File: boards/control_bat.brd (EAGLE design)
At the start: 102.6 x 30.5 mm, 13 parts, among them U1 MCP1703T-3002E/CB, U3 LPC824M201JDH20J, X2 53398-04

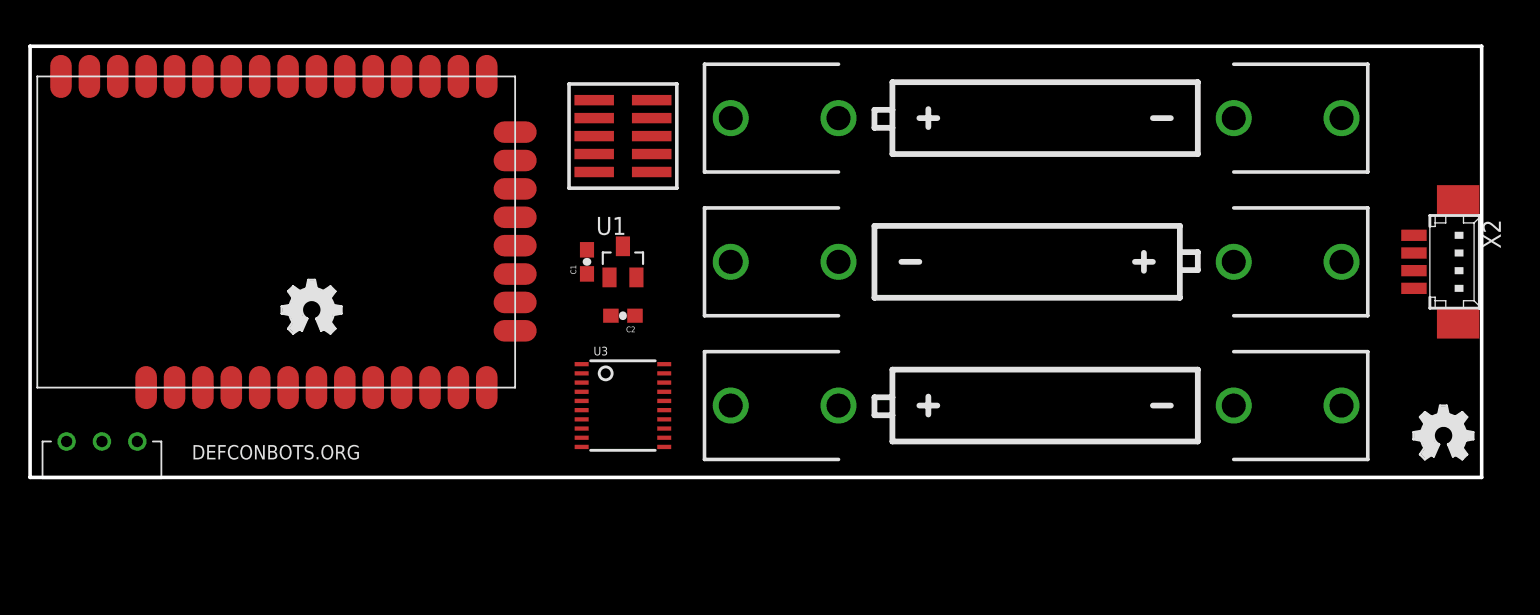
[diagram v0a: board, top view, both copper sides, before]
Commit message: First pass layout of control/battery board
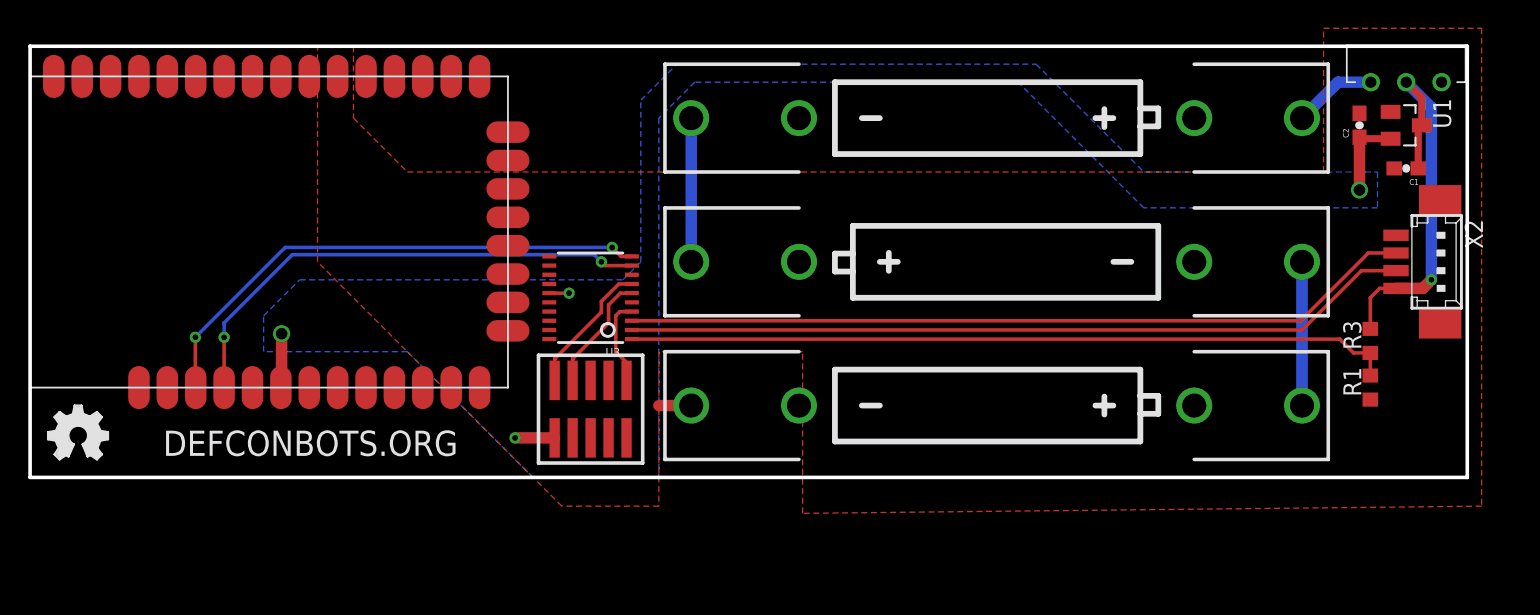
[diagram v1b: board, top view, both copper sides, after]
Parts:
- removed LOGO2: OSHW_LOGO_FILLX0150-NT, ohw-logo:OSHW_FILLX150_NOTEXT
- added R1, R3: 10k, rcl:R0603
- moved LOGO1 96.5 mm to (1.27, 1.27)
- moved S3 95.6 mm to (97.3, 27.9), turned to 90 degrees
- moved C1 58.3 mm to (97.3, 21.8), turned to 180 degrees
- moved U1 56.2 mm to (97.3, 24.9), turned to 270 degrees
- moved C2 53.8 mm to (94.0, 24.9), turned to 90 degrees
- moved BAT1 20.5 mm to (68.3, 5.08), turned to 180 degrees
- moved BAT3 20.5 mm to (68.3, 25.4), turned to 180 degrees
- moved U$3 19.4 mm to (39.6, 4.83), turned to 0 degrees
- moved U3 7.96 mm to (39.6, 12.7), turned to 90 degrees
- moved BAT2 2.79 mm to (68.3, 15.2), turned to 0 degrees
- moved X2 1.27 mm to (99.1, 15.2)
- moved XB1 0.51 mm to (33.8, 6.35)
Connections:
- removed net BLUE_LED: U3.1
- removed net LASER_RX: U3.3
- removed net RED_LED: U3.10
- new net N$3: BAT3.PWR@1, S3.P$1
- new net RF_RX: U3.10, XB1.3
- new net RF_TX: U3.9, XB1.4
- net +3V3: now also XB1.6
- net GND: now also R1.1, XB1.27
- net RX: now also U3.3; no longer U3.8
- net TX: now also U3.2; no longer U3.9
- net VBAT: now also R1.2, R3.1, U3.1; no longer BAT3.PWR@1, S3.P$2
- net VIN: now also R3.2, S3.P$2; no longer S3.P$1
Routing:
- net RX: track 0.00 -> 56.0 mm
- net TX: track 0.00 -> 55.8 mm
- net VBAT: track 0.00 -> 54.2 mm
- net RF_RX: track 0.00 -> 37.3 mm, vias 0 -> 2
- net RF_TX: track 0.00 -> 35.7 mm, vias 0 -> 2
- net VIN: track 0.00 -> 28.4 mm, vias 0 -> 1
- net +3V3: track 0.00 -> 14.0 mm, vias 0 -> 4
- net N$1: track 0.00 -> 10.2 mm
- net N$2: track 0.00 -> 10.2 mm
- net SWDIO: track 0.00 -> 9.62 mm
- net SWCLK: track 0.00 -> 8.38 mm
- net RST: track 0.00 -> 6.15 mm
- net N$3: track 0.00 -> 5.92 mm
- net GND: track 0.00 -> 2.29 mm
- added copper zone on layer 16, net +3V3
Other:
- board size 102.6 x 30.5 mm -> 101.6 x 30.5 mm

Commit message: Add serial debug port on xbee in case I need to configure it manually
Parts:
- added JP1: (no value), SparkFun-Connectors:1X03
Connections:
- net RF_RX: now also JP1.1
- net RF_TX: now also JP1.2
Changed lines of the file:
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@@
 <layer number="98" name="Guide" color="6" fill="1" visible="no" active="no"/>
 <layer number="99" name="SpiceOrder" color="7" fill="1" visible="no" active="no"/>
+<layer number="100" name="Muster" color="7" fill="1" visible="no" active="no"/>
+<layer number="101" name="Patch_Top" color="12" fill="4" visible="no" active="yes"/>
+<layer number="102" name="Vscore" color="7" fill="1" visible="no" active="yes"/>
+<layer number="103" name="tMap" color="7" fill="1" visible="no" active="yes"/>
+<layer number="104" name="Name" color="16" fill="1" visible="no" active="yes"/>
+<layer number="105" name="tPlate" color="7" fill="1" visible="no" active="yes"/>
+<layer number="106" name="bPlate" color="7" fill="1" visible="no" active="yes"/>
+<layer number="107" name="Crop" color="7" fill="1" visible="no" active="yes"/>
+<layer number="108" name="tplace-old" color="10" fill="1" visible="no" active="yes"/>
+<layer number="109" name="ref-old" color="11" fill="1" visible="no" active="yes"/>
+<layer number="110" name="fp0" color="7" fill="1" visible="no" active="yes"/>
 <layer number="111" name="Route11" color="7" fill="1" visible="no" active="no"/>
 <layer number="112" name="Route12" color="7" fill="1" visible="no" active="no"/>
@@
 <layer number="114" name="Route14" color="7" fill="1" visible="no" active="no"/>
 <layer number="115" name="Route15" color="7" fill="1" visible="no" active="no"/>
+<layer number="116" name="Patch_BOT" color="9" fill="4" visible="no" active="yes"/>
+<layer number="121" name="_tsilk" color="7" fill="1" visible="no" active="yes"/>
+<layer number="122" name="_bsilk" color="7" fill="1" visible="no" active="yes"/>
+<layer number="123" name="tTestmark" color="7" fill="1" visible="no" active="yes"/>
+<layer number="124" name="bTestmark" color="7" fill="1" visible="no" active="yes"/>
+<layer number="125" name="_tNames" color="7" fill="1" visible="no" active="yes"/>
+<layer number="126" name="_bNames" color="7" fill="1" visible="no" active="yes"/>
+<layer number="127" name="_tValues" color="7" fill="1" visible="no" active="yes"/>
+<layer number="128" name="_bValues" color="7" fill="1" visible="no" active="yes"/>
+<layer number="131" name="tAdjust" color="7" fill="1" visible="no" active="yes"/>
+<layer number="132" name="bAdjust" color="7" fill="1" visible="no" active="yes"/>
+<layer number="144" name="Drill_legend" color="7" fill="1" visible="no" active="yes"/>
+<layer number="150" name="Notes" color="7" fill="1" visible="no" active="yes"/>
+<layer number="151" name="HeatSink" color="7" fill="1" visible="no" active="yes"/>
+<layer number="152" name="_bDocu" color="7" fill="1" visible="no" active="yes"/>
+<layer number="153" name="FabDoc1" color="7" fill="1" visible="no" active="yes"/>
+<layer number="154" name="FabDoc2" color="7" fill="1" visible="no" active="yes"/>
+<layer number="155" name="FabDoc3" color="7" fill="1" visible="no" active="yes"/>
+<layer number="199" name="Contour" color="7" fill="1" visible="no" active="yes"/>
 <layer number="200" name="200bmp" color="1" fill="10" visible="no" active="no"/>
+<layer number="201" name="201bmp" color="2" fill="10" visible="no" active="yes"/>
+<layer number="202" name="202bmp" color="3" fill="10" visible="no" active="yes"/>
+<layer number="203" name="203bmp" color="4" fill="10" visible="no" active="yes"/>
+<layer number="204" name="204bmp" color="5" fill="10" visible="no" active="yes"/>
+<layer number="205" name="205bmp" color="6" fill="10" visible="no" active="yes"/>
+<layer number="206" name="206bmp" color="7" fill="10" visible="no" active="yes"/>
+<layer number="207" name="207bmp" color="8" fill="10" visible="no" active="yes"/>
+<layer number="208" name="208bmp" color="9" fill="10" visible="no" active="yes"/>
+<layer number="209" name="209bmp" color="7" fill="1" visible="no" active="yes"/>
+<layer number="210" name="210bmp" color="7" fill="1" visible="no" active="yes"/>
+<layer number="211" name="211bmp" color="7" fill="1" visible="no" active="yes"/>
+<layer number="212" name="212bmp" color="7" fill="1" visible="no" active="yes"/>
+<layer number="213" name="213bmp" color="7" fill="1" visible="no" active="yes"/>
+<layer number="214" name="214bmp" color="7" fill="1" visible="no" active="yes"/>
+<layer number="215" name="215bmp" color="7" fill="1" visible="no" active="yes"/>
+<layer number="216" name="216bmp" color="7" fill="1" visible="no" active="yes"/>
 <layer number="217" name="217bmp" color="18" fill="1" visible="no" active="no"/>
 <layer number="218" name="218bmp" color="19" fill="1" visible="no" active="no"/>
@@
 <layer number="223" name="223bmp" color="24" fill="1" visible="no" active="no"/>
 <layer number="224" name="224bmp" color="25" fill="1" visible="no" active="no"/>
+<layer number="248" name="Housing" color="7" fill="1" visible="no" active="yes"/>
+<layer number="249" name="Edge" color="7" fill="1" visible="no" active="yes"/>
 <layer number="250" name="Descript" color="3" fill="1" visible="no" active="no"/>
 <layer number="251" name="SMDround" color="12" fill="11" visible="no" active="no"/>
+<layer number="254" name="cooling" color="7" fill="1" visible="no" active="yes"/>
 </layers>
 <board>
@@
 <wire x1="101.6" y1="30.48" x2="0" y2="30.48" width="0.254" layer="20"/>
 <wire x1="0" y1="30.48" x2="0" y2="0" width="0.254" layer="20"/>
-<text x="9.398" y="1.524" size="1.778" layer="21" font="vector" ratio="10">DEFCONBOTS.ORG</text>
+<text x="5.588" y="20.574" size="1.778" layer="21" font="vector" ratio="10">DEFCONBOTS.ORG</text>
 </plain>
 <attributes>
@@
 <element name="R3" library="rcl" package="R0603" value="10k" x="94.742" y="9.652" rot="R90"/>
 <element name="R1" library="rcl" package="R0603" value="10k" x="94.742" y="6.35" rot="R90"/>
+<element name="JP1" library="SparkFun-Connectors" package="1X03" value="" x="2.54" y="-6.35"/>
 </elements>
 <signals>
@@
 <via x="13.716" y="9.906" extent="1-16" drill="0.4064"/>
 <wire x1="13.716" y1="9.906" x2="13.716" y2="6.35" width="0.254" layer="1"/>
+<contactref element="JP1" pad="2"/>
+<wire x1="5.08" y1="-6.35" x2="13.716" y2="6.35" width="0" layer="19" extent="1-1"/>
 </signal>
 <signal name="RF_RX">
@@
 <wire x1="11.684" y1="9.906" x2="11.684" y2="6.3754" width="0.254" layer="1"/>
 <wire x1="11.684" y1="6.3754" x2="11.7094" y2="6.35" width="0.254" layer="1"/>
+<contactref element="JP1" pad="1"/>
+<wire x1="2.54" y1="-6.35" x2="11.7094" y2="6.35" width="0" layer="19" extent="1-1"/>
 </signal>
 <signal name="VBAT">

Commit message: Some ground plane improvements
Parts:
- moved JP1 12.6 mm to (11.4, 2.54)
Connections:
- net GND: now also JP1.3
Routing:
- net RF_RX: track 37.3 -> 41.2 mm
- net RF_TX: track 35.7 -> 39.6 mm
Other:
- board text added: "2015 Controller"
- board text added: "R1"
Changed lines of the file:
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@@
 <wire x1="101.6" y1="30.48" x2="0" y2="30.48" width="0.254" layer="20"/>
 <wire x1="0" y1="30.48" x2="0" y2="0" width="0.254" layer="20"/>
-<text x="5.588" y="20.574" size="1.778" layer="21" font="vector" ratio="10">DEFCONBOTS.ORG</text>
+<text x="19.05" y="1.27" size="1.016" layer="21" font="vector" ratio="10">DEFCONBOTS.ORG</text>
+<text x="19.05" y="2.54" size="1.016" layer="21">2015 Controller</text>
+<text x="29.21" y="2.54" size="1.016" layer="21">R1</text>
 </plain>
 <attributes>
@@
 <element name="R3" library="rcl" package="R0603" value="10k" x="94.742" y="9.652" rot="R90"/>
 <element name="R1" library="rcl" package="R0603" value="10k" x="94.742" y="6.35" rot="R90"/>
-<element name="JP1" library="SparkFun-Connectors" package="1X03" value="" x="2.54" y="-6.35"/>
+<element name="JP1" library="SparkFun-Connectors" package="1X03" value="" x="11.43" y="2.54"/>
 </elements>
 <signals>
@@
 <vertex x="26.67" y="21.59"/>
 <vertex x="91.44" y="21.59"/>
-<vertex x="91.44" y="31.75"/>
-<vertex x="102.616" y="31.75"/>
-<vertex x="102.616" y="-2.032"/>
+<vertex x="91.44" y="27.94"/>
+<vertex x="101.6" y="27.94"/>
+<vertex x="101.6" y="-2.54"/>
 <vertex x="54.61" y="-2.54"/>
 <vertex x="54.61" y="8.89"/>
 <vertex x="44.45" y="8.89"/>
-<vertex x="44.45" y="-2.032"/>
-<vertex x="37.592" y="-2.032"/>
-<vertex x="20.32" y="15.24"/>
+<vertex x="44.45" y="-2.54"/>
+<vertex x="15.24" y="-2.54"/>
+<vertex x="15.24" y="5.08"/>
+<vertex x="20.32" y="5.08"/>
 </polygon>
 <wire x1="46.736" y1="5.08" x2="44.45" y2="5.08" width="0.8128" layer="1"/>
+<contactref element="JP1" pad="3"/>
 </signal>
 <signal name="+3V3">
@@
 <wire x1="13.716" y1="9.906" x2="13.716" y2="6.35" width="0.254" layer="1"/>
 <contactref element="JP1" pad="2"/>
-<wire x1="5.08" y1="-6.35" x2="13.716" y2="6.35" width="0" layer="19" extent="1-1"/>
+<wire x1="13.716" y1="6.35" x2="13.716" y2="2.794" width="0.254" layer="1"/>
+<wire x1="13.716" y1="2.794" x2="13.97" y2="2.54" width="0.254" layer="1"/>
 </signal>
 <signal name="RF_RX">
@@
 <wire x1="11.684" y1="6.3754" x2="11.7094" y2="6.35" width="0.254" layer="1"/>
 <contactref element="JP1" pad="1"/>
-<wire x1="2.54" y1="-6.35" x2="11.7094" y2="6.35" width="0" layer="19" extent="1-1"/>
+<wire x1="11.7094" y1="6.35" x2="11.7094" y2="2.8194" width="0.254" layer="1"/>
+<wire x1="11.7094" y1="2.8194" x2="11.43" y2="2.54" width="0.254" layer="1"/>
 </signal>
 <signal name="VBAT">

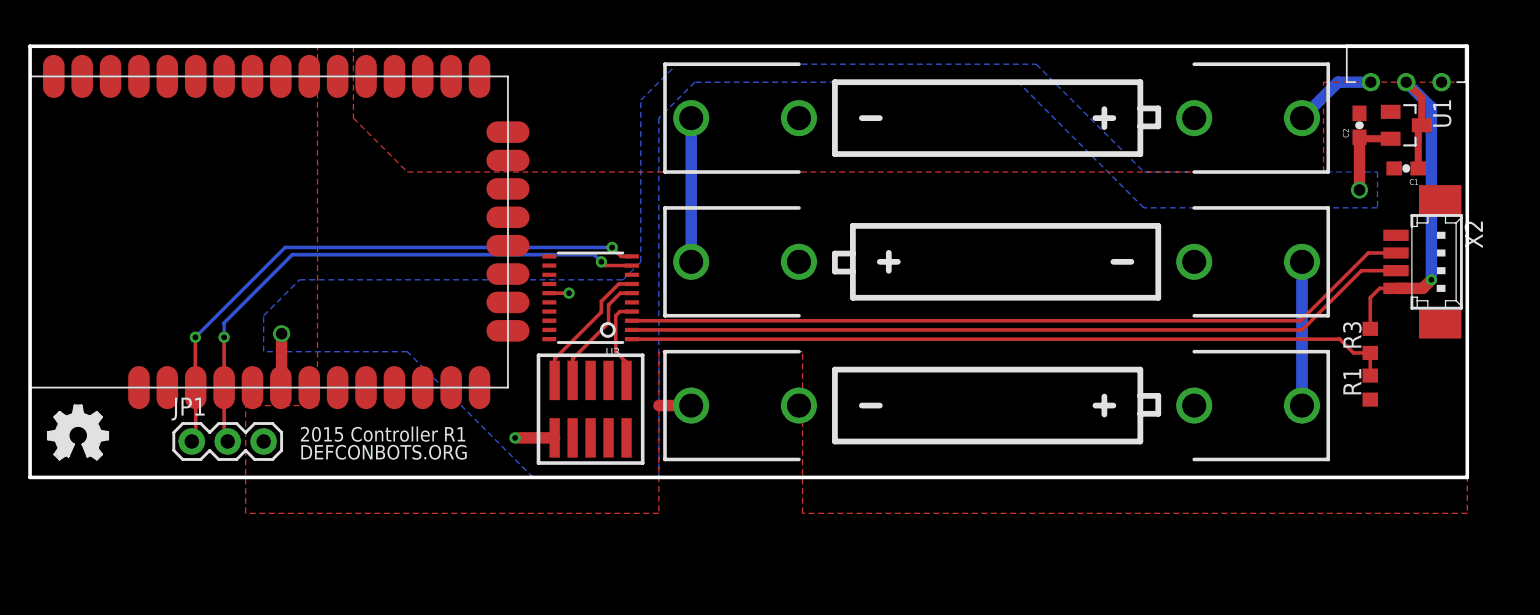
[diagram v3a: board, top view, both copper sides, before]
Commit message: Fix footprint (was footprint for LPC812 instead of LPC824). Update part numbers on the schematic. Add IR. Cleanup ground plane.
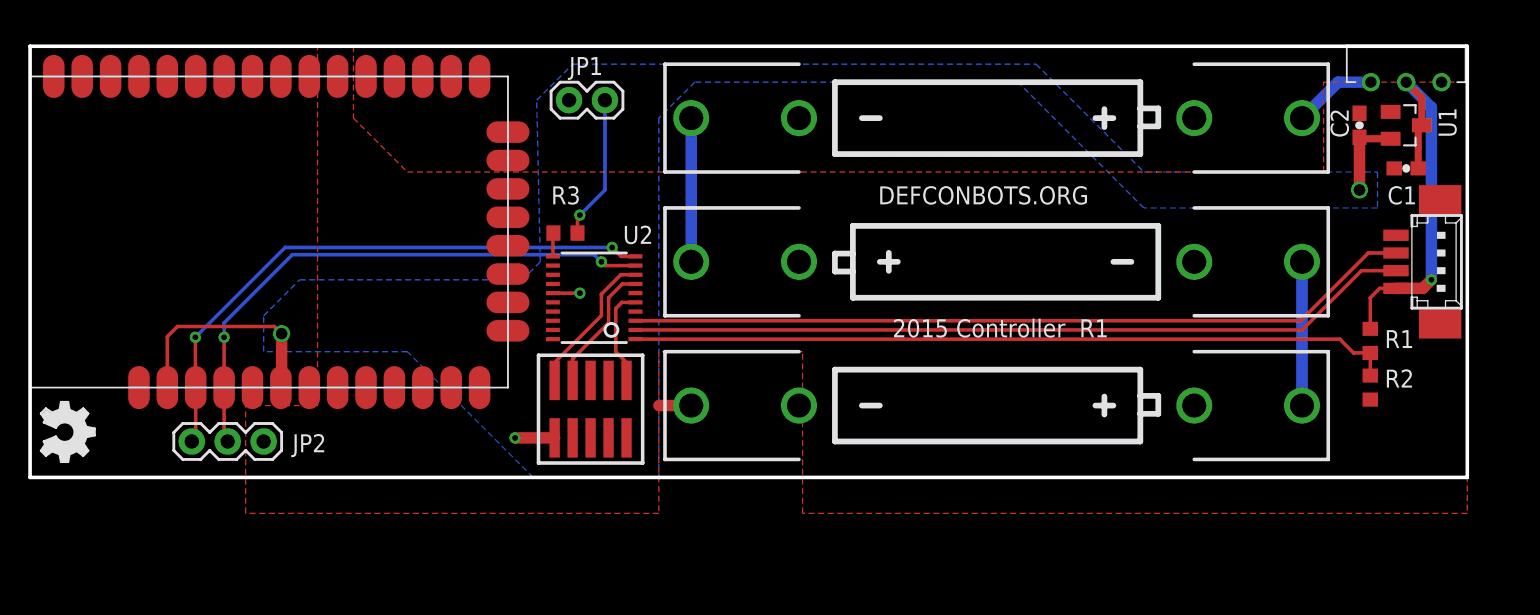
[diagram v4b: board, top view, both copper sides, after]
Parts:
- removed XB1: 888-XB24CZ7PIS-004, xbee:XBEE-SMT
- added JP2: (no value), SparkFun-Connectors:1X03
- added R2: 71-CRCW0603-10K-E3, rcl:R0603
- added U2: 771-LPC824M201JDH20J, torpedo:TSSOP20
- JP1: device SparkFun-Connectors:1X03 -> SparkFun-Connectors:1X02
- JP3: value FTSH-105 -> FTSH-105-01-L
- JP4: value 53398-04 -> 798-DF134P125V20
- R1: value 10k -> 71-CRCW0603-10K-E3
- R3: value 10k -> 71-CRCW0603220RFKEB
- S1: value (none) -> 612-EG1270
- U1: value MCP1703T-3002E/CB -> 579-MCP1703T-3002ECB
- U3: value LPC824M201JDH20J -> 888-XB24CZ7PIS-004; device LPC800:TSSOP20 -> xbee:XBEE-SMT
- moved R3 57.4 mm to (37.8, 17.3), turned to 0 degrees
- moved JP1 36.0 mm to (38.1, 26.7)
- moved BAT1 20.3 mm to (68.3, 25.4)
- moved BAT3 20.3 mm to (68.3, 5.08)
- moved U3 8.63 mm to (33.8, 6.35)
- moved LOGO1 4.10 mm to (0.76, 5.33), turned to 270 degrees
- moved R1 3.30 mm to (94.7, 9.65)
- renumbered S3 to S1, U$3 to JP3, X2 to JP4
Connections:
- new net IR: R3.1, U2.11
- new net N$4: JP1.2, R3.2
- net +3V3: now also JP1.1, U2.15, U3.2, U3.6; no longer U3.15, XB1.2, XB1.6
- net GND: now also BAT3.GND@1, JP2.3, R2.1, U2.16, U3.13, U3.27; no longer BAT1.GND@1, JP1.3, R1.1, U3.16, XB1.13, XB1.27
- net N$1: now also BAT3.PWR@1; no longer BAT1.PWR@1
- net N$2: now also BAT1.GND@1; no longer BAT3.GND@1
- net N$3: now also BAT1.PWR@1; no longer BAT3.PWR@1
- net RF_RX: now also JP2.1, U2.10, U3.3; no longer JP1.1, U3.10, XB1.3
- net RF_TX: now also JP2.2, U2.9, U3.4; no longer JP1.2, U3.9, XB1.4
- net RST: now also U2.5; no longer U3.4
- net RX: now also U2.3; no longer U3.3
- net SWCLK: now also U2.7; no longer U3.6
- net SWDIO: now also U2.8; no longer U3.7
- net TX: now also U2.2; no longer U3.2
- net VBAT: now also R1.1, R2.2, U2.1; no longer R1.2, R3.1, U3.1
- net VIN: now also R1.2; no longer R3.2
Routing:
- net +3V3: track 14.0 -> 26.7 mm
- net N$4: track 0.00 -> 10.2 mm, vias 0 -> 1
- net IR: track 0.00 -> 1.66 mm
- net RST: track 6.15 -> 6.97 mm
- net SWDIO: track 9.62 -> 10.4 mm
- net SWCLK: track 8.38 -> 9.20 mm
